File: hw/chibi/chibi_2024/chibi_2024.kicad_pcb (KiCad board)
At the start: 2 copper layers, 100 x 78 mm, 95 parts, among them P1 VIN, P2 VIN, P3 GND, P4 CONN_02X03, P5 SWD, P6 GND, Q1 AO3415A, Q14 Q_PNP_BEC, Q15 Q_NPN_BEC, Q16 Q_NPN_BEC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

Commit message: Second production run, v0.3
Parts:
- svg2mod: footprint footprints:label_data_v01 -> footprints:label_data_02

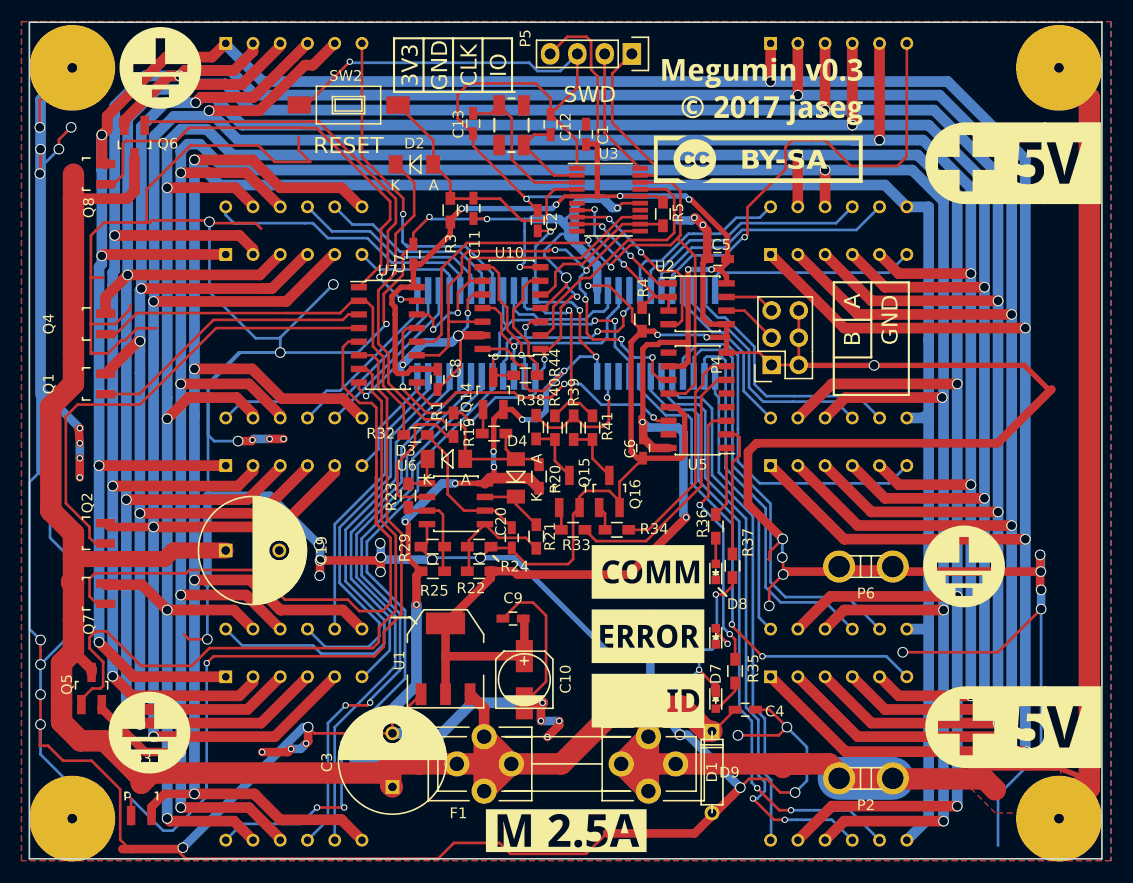
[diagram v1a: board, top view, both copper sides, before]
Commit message: Fixes for second prototype (v0.3)
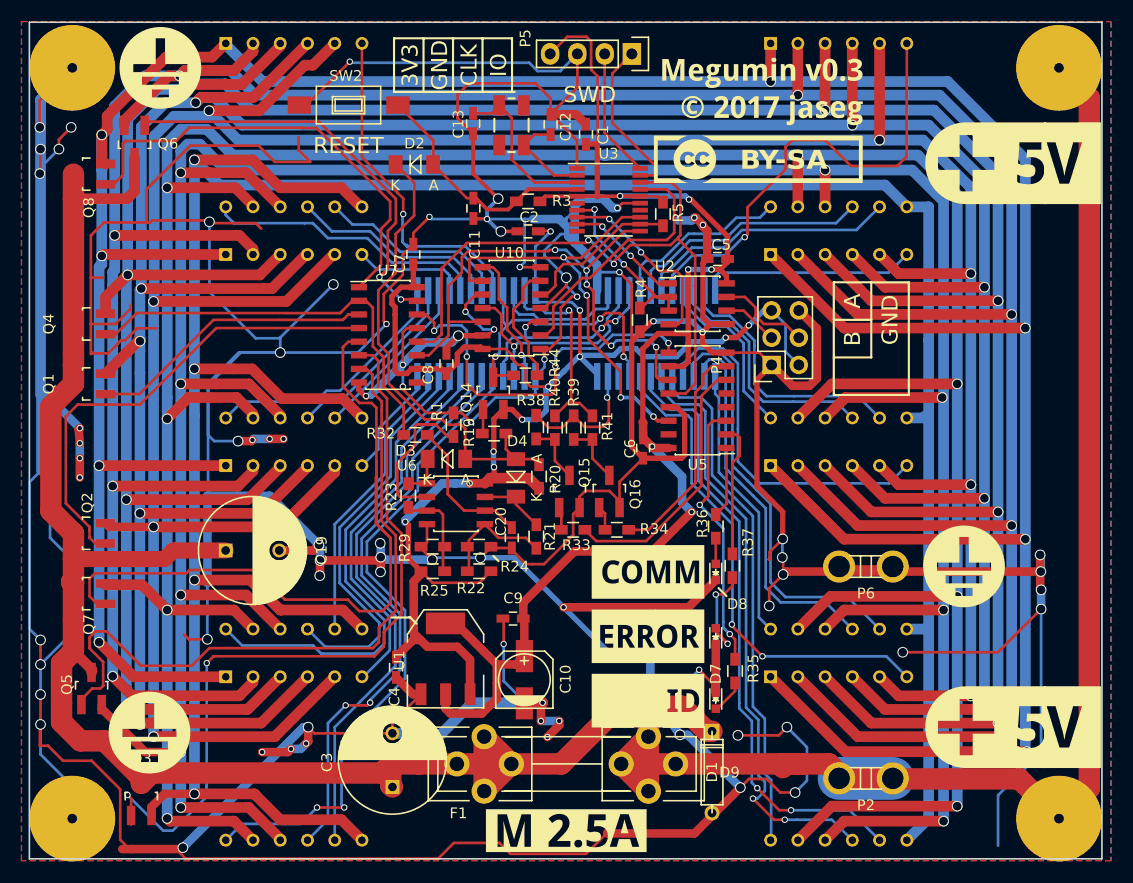
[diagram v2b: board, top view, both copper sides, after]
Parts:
- moved C4 32.8 mm to (83.2, 103.9), turned to 90 degrees
- moved R3 7.30 mm to (95.5, 60.5), turned to 180 degrees
- moved C8 1.70 mm to (87.9, 75.6), turned to 270 degrees
- moved C2 1.34 mm to (95.5, 63.2), turned to 0 degrees
- moved R4 0.21 mm to (105.9, 71.5)
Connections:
- C2 pad 2: VDD -> +5V
- C4 pad 2: VDD -> +5V
- C7 pad 2: +3V3 -> +5V
- C8 pad 2: +3V3 -> +5V
- P4 pad 2: GND -> +5V
- P4 pad 4: GND -> /RS485_B
- P4 pad 5: /RS485_B -> +5V
- Q14 pad 2: VDD -> +5V
- R20 pad 1: VDD -> +5V
- R22 pad 2: +3V3 -> +5V
- R25 pad 2: VDD -> +5V
- U1 pad 3: VDD -> +5V
- U10 pad 14: VDD -> +5V
- U5 pad 14: Net-(U5-Pad14) -> /MOSI_C0
- U5 pad 9: Net-(U5-Pad9) -> /MOSI_C2
- U6 pad 8: VDD -> +5V
- U7 pad 10: +3V3 -> +5V
- U7 pad 14: /MOSI_C0 -> /MOSI_C2
- U7 pad 16: +3V3 -> +5V
- U7 pad 9: Net-(U5-Pad14) -> Net-(U7-Pad9)
- U8 pad 24: VDD -> +5V
- U9 pad 24: VDD -> +5V
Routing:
- net +5V: track 0.00 -> 148.3 mm, vias 0 -> 11
- net VDD: track 282.8 -> 167.6 mm, vias 10 -> 0
- net +3V3: track 211.3 -> 153.1 mm, vias 8 -> 6
- net /MOSI_C2: track 0.00 -> 36.9 mm, vias 0 -> 4
- net Net-(U5-Pad14): track 27.4 -> 0.00 mm, vias 2 -> 0
- net GND: track 1011.3 -> 986.7 mm, vias 78 -> 81
- net /MOSI_C0: track 29.8 -> 42.2 mm, vias 2 -> 4
- net /VDD_PRE_FUSE: track 159.3 -> 150.5 mm
- net /RS485_B: track 4.72 -> 8.76 mm
- net /RST: track 26.2 -> 23.2 mm
- net /MOSI_C1_HV: track 12.9 -> 14.5 mm
- net /~OE_HV_CB: track 27.4 -> 28.6 mm
- net Net-(D11-Pad6): track 35.0 -> 34.0 mm
- net Net-(D11-Pad8): track 40.3 -> 39.4 mm
- net /SCK: track 52.2 -> 53.0 mm
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- removed copper zone on F.Cu, net /VDD_PRE_FUSE

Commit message: Fix up version label and one ground trace
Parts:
- svg2mod: footprint footprints:label_data_02 -> footprints:label_data_04
- moved svg2mod 3.42 mm to (119.0, 52.3)
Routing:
- net GND: track 986.7 -> 995.5 mm, vias 81 -> 85
- net /VDD_PRE_FUSE: track 150.5 -> 146.8 mm
